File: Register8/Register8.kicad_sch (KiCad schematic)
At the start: 23 parts, among them J1 Conn_01x08, J2 Conn_01x08, J3 Conn_01x08, J4 Conn_01x08, J5 Conn_01x04, J6 Conn_01x04, J7 Conn_01x02, J8 Conn_01x02, U1 74HC245, U2 74LS173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

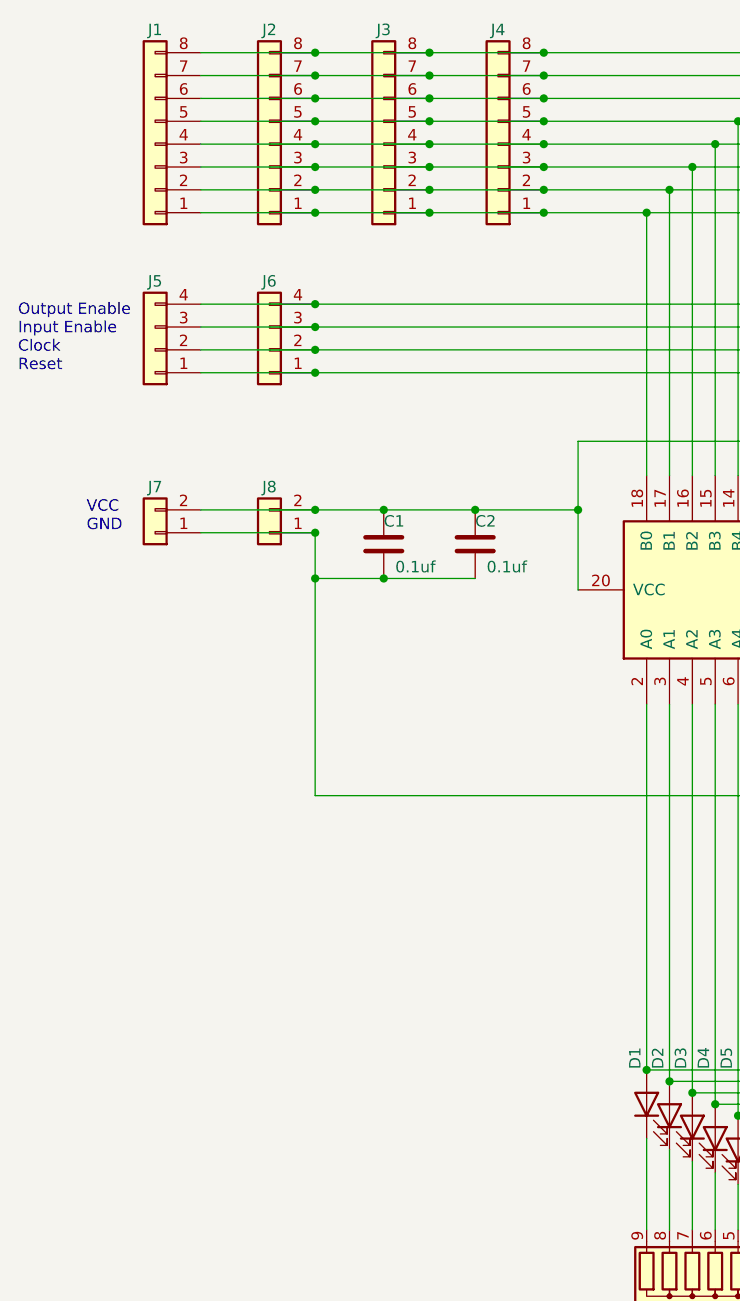
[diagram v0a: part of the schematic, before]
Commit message: Made Register 8bit pcb
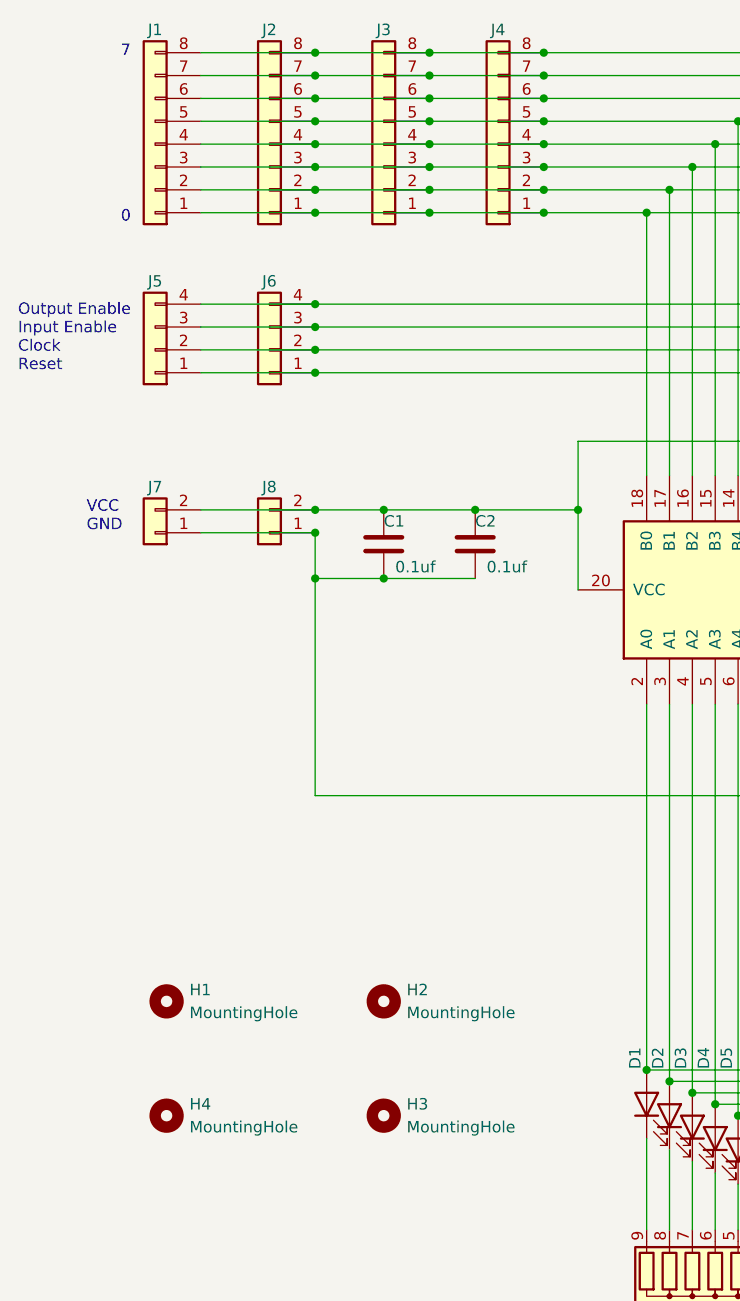
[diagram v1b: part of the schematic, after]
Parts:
- added H1, H2, H3, H4: MountingHole, MountingHole:MountingHole_3.2mm_M3, symbol Mechanical:MountingHole
- D1, D2, D3, D4, D5, D6, D7, D8: footprint LED_THT:LED_D5.0mm-3 -> LED_THT:LED_D5.0mm
- U1: footprint Package_SO:SOIC-14W_7.5x9mm_P1.27mm -> Package_SO:SOIC-20W_7.5x12.8mm_P1.27mm
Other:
- note added: "7 0"
- title: (none) -> Register 8bit
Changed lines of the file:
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@@
 (kicad_sch (version 20230121) (generator eeschema)
   (paper "A4")
+  (title_block
+    (title "Register 8bit")
+    (date "2023-08-31")
+    (rev "0")
+  )
   (junction (at 73.66 39.37) (diameter 0) (color 0 0 0 0)
   )
@@
     (effects (font (size 1.27 1.27)) (justify left bottom))
   )
+  (text "7\n\n\n\n\n\n\n\n\n0" (at 26.67 50.8 0)
+    (effects (font (size 1.27 1.27)) (justify left bottom))
+  )
   (text "Output Enable\nInput Enable\nClock\nReset" (at 15.24 67.31 0)
     (effects (font (size 1.27 1.27)) (justify left bottom))
+  )
+  (symbol (lib_id "Mechanical:MountingHole") (at 31.75 149.86 0) (unit 1)
+    (in_bom yes) (on_board yes) (dnp no) (fields_autoplaced)
+    (property "Reference" "H4" (at 34.29 148.59 0)
+      (effects (font (size 1.27 1.27)) (justify left))
+    )
+    (property "Value" "MountingHole" (at 34.29 151.13 0)
+      (effects (font (size 1.27 1.27)) (justify left))
+    )
+    (property "Footprint" "MountingHole:MountingHole_3.2mm_M3" (at 31.75 149.86 0)
+      (effects (font (size 1.27 1.27)) hide)
+    )
+    (property "Datasheet" "~" (at 31.75 149.86 0)
+      (effects (font (size 1.27 1.27)) hide)
+    )
+    (instances
+      (project "Register8"
+        (path "/5cfd5bcb-044d-4fc2-a5e2-246a2c9e17c3"
+          (reference "H4") (unit 1)
+        )
+      )
+    )
   )
   (symbol (lib_id "74xx:74LS173") (at 170.18 95.25 270) (unit 1)
@@
     )
   )
+  (symbol (lib_id "Mechanical:MountingHole") (at 31.75 137.16 0) (unit 1)
+    (in_bom yes) (on_board yes) (dnp no) (fields_autoplaced)
+    (property "Reference" "H1" (at 34.29 135.89 0)
+      (effects (font (size 1.27 1.27)) (justify left))
+    )
+    (property "Value" "MountingHole" (at 34.29 138.43 0)
+      (effects (font (size 1.27 1.27)) (justify left))
+    )
+    (property "Footprint" "MountingHole:MountingHole_3.2mm_M3" (at 31.75 137.16 0)
+      (effects (font (size 1.27 1.27)) hide)
+    )
+    (property "Datasheet" "~" (at 31.75 137.16 0)
+      (effects (font (size 1.27 1.27)) hide)
+    )
+    (instances
+      (project "Register8"
+        (path "/5cfd5bcb-044d-4fc2-a5e2-246a2c9e17c3"
+          (reference "H1") (unit 1)
+        )
+      )
+    )
+  )
   (symbol (lib_id "Device:LED") (at 85.09 148.59 90) (unit 1)
     (in_bom yes) (on_board yes) (dnp no)
@@
       (effects (font (size 1.27 1.27)) (justify right) hide)
     )
-    (property "Footprint" "LED_THT:LED_D5.0mm-3" (at 85.09 148.59 0)
+    (property "Footprint" "LED_THT:LED_D5.0mm" (at 85.09 148.59 0)
       (effects (font (size 1.27 1.27)) hide)
     )
@@
       (effects (font (size 1.27 1.27)))
     )
-    (property "Footprint" "Package_SO:SOIC-14W_7.5x9mm_P1.27mm" (at 97.79 91.44 0)
+    (property "Footprint" "Package_SO:SOIC-20W_7.5x12.8mm_P1.27mm" (at 97.79 91.44 0)
       (effects (font (size 1.27 1.27)) hide)
     )
@@
       (effects (font (size 1.27 1.27)) (justify right) hide)
     )
-    (property "Footprint" "LED_THT:LED_D5.0mm-3" (at 97.79 154.94 0)
+    (property "Footprint" "LED_THT:LED_D5.0mm" (at 97.79 154.94 0)
       (effects (font (size 1.27 1.27)) hide)
     )
@@
       (effects (font (size 1.27 1.27)) (justify right) hide)
     )
-    (property "Footprint" "LED_THT:LED_D5.0mm-3" (at 87.63 149.86 0)
+    (property "Footprint" "LED_THT:LED_D5.0mm" (at 87.63 149.86 0)
       (effects (font (size 1.27 1.27)) hide)
     )
@@
         (path "/5cfd5bcb-044d-4fc2-a5e2-246a2c9e17c3"
           (reference "D2") (unit 1)
+        )
+      )
+    )
+  )
+  (symbol (lib_id "Mechanical:MountingHole") (at 55.88 137.16 0) (unit 1)
+    (in_bom yes) (on_board yes) (dnp no) (fields_autoplaced)
+    (property "Reference" "H2" (at 58.42 135.89 0)
+      (effects (font (size 1.27 1.27)) (justify left))
+    )
+    (property "Value" "MountingHole" (at 58.42 138.43 0)
+      (effects (font (size 1.27 1.27)) (justify left))
+    )
+    (property "Footprint" "MountingHole:MountingHole_3.2mm_M3" (at 55.88 137.16 0)
+      (effects (font (size 1.27 1.27)) hide)
+    )
+    (property "Datasheet" "~" (at 55.88 137.16 0)
+      (effects (font (size 1.27 1.27)) hide)
+    )
+    (instances
+      (project "Register8"
+        (path "/5cfd5bcb-044d-4fc2-a5e2-246a2c9e17c3"
+          (reference "H2") (unit 1)
         )
       )
@@
         (path "/5cfd5bcb-044d-4fc2-a5e2-246a2c9e17c3"
           (reference "J6") (unit 1)
+        )
+      )
+    )
+  )
+  (symbol (lib_id "Mechanical:MountingHole") (at 55.88 149.86 0) (unit 1)
+    (in_bom yes) (on_board yes) (dnp no) (fields_autoplaced)
+    (property "Reference" "H3" (at 58.42 148.59 0)
+      (effects (font (size 1.27 1.27)) (justify left))
+    )
+    (property "Value" "MountingHole" (at 58.42 151.13 0)
+      (effects (font (size 1.27 1.27)) (justify left))
+    )
+    (property "Footprint" "MountingHole:MountingHole_3.2mm_M3" (at 55.88 149.86 0)
+      (effects (font (size 1.27 1.27)) hide)
+    )
+    (property "Datasheet" "~" (at 55.88 149.86 0)
+      (effects (font (size 1.27 1.27)) hide)
+    )
+    (instances
+      (project "Register8"
+        (path "/5cfd5bcb-044d-4fc2-a5e2-246a2c9e17c3"
+          (reference "H3") (unit 1)
         )
       )
@@
       (effects (font (size 1.27 1.27)) (justify right) hide)
     )
-    (property "Footprint" "LED_THT:LED_D5.0mm-3" (at 92.71 152.4 0)
+    (property "Footprint" "LED_THT:LED_D5.0mm" (at 92.71 152.4 0)
       (effects (font (size 1.27 1.27)) hide)
     )
@@
       (effects (font (size 1.27 1.27)) (justify right) hide)
     )
-    (property "Footprint" "LED_THT:LED_D5.0mm-3" (at 90.17 151.13 0)
+    (property "Footprint" "LED_THT:LED_D5.0mm" (at 90.17 151.13 0)
       (effects (font (size 1.27 1.27)) hide)
     )
@@
       (effects (font (size 1.27 1.27)) (justify right) hide)
     )
-    (property "Footprint" "LED_THT:LED_D5.0mm-3" (at 102.87 158.75 0)
+    (property "Footprint" "LED_THT:LED_D5.0mm" (at 102.87 158.75 0)
       (effects (font (size 1.27 1.27)) hide)
     )
@@
       (effects (font (size 1.27 1.27)) (justify right) hide)
     )
-    (property "Footprint" "LED_THT:LED_D5.0mm-3" (at 95.25 153.67 0)
+    (property "Footprint" "LED_THT:LED_D5.0mm" (at 95.25 153.67 0)
       (effects (font (size 1.27 1.27)) hide)
     )
@@
       (effects (font (size 1.27 1.27)) (justify right) hide)
     )
-    (property "Footprint" "LED_THT:LED_D5.0mm-3" (at 100.33 156.21 0)
-      (effects (font (size 1.27 1.27)) hide)
-    )
+    (property "Footprint" "LED_THT:LED_D5.0mm" (at 100.33 156.21 0)
+      (effects (font (size 1.27 1.27)) hide)
+    )
